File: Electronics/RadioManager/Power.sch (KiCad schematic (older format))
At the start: 10 parts

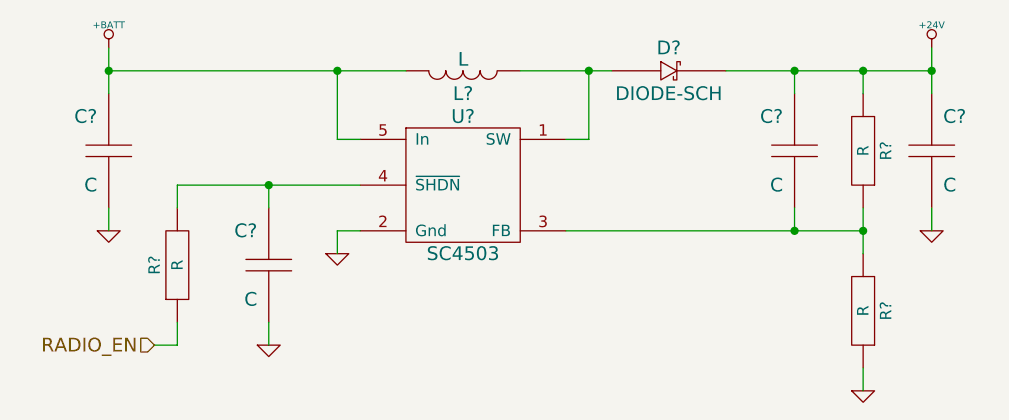
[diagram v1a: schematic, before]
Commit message: Annotate existing components
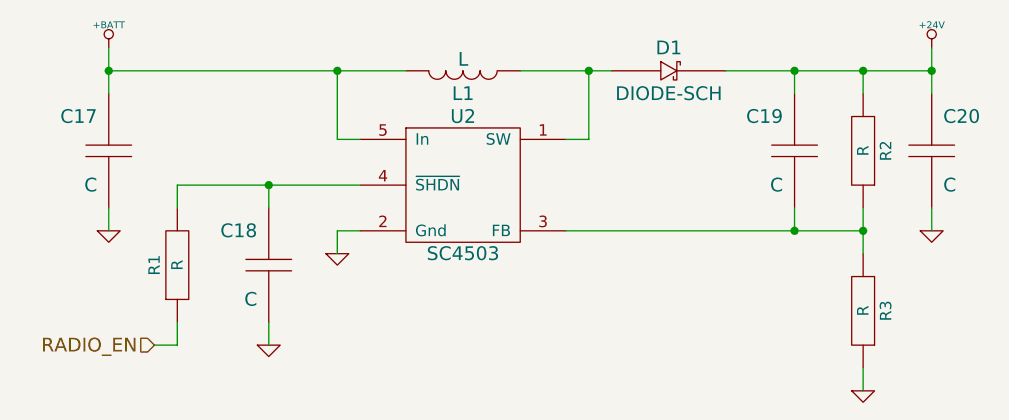
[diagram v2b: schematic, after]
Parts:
- gave numbers to parts that had none: 10
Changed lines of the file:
@@
 $EndDescr
 $Comp
-L SC4503 U?
+L SC4503 U2
 U 1 1 5410EB93
 P 3050 1900
-F 0 "U?" H 3050 2200 60  0000 C CNN
+F 0 "U2" H 3050 2200 60  0000 C CNN
 F 1 "SC4503" H 3050 1600 60  0000 C CNN
 F 2 "" H 3050 1900 60  0000 C CNN
@@
 $EndComp
 $Comp
-L L L?
+L L L1
 U 1 1 5410EB99
 P 3050 1400
-F 0 "L?" H 3050 1300 60  0000 C CNN
+F 0 "L1" H 3050 1300 60  0000 C CNN
 F 1 "L" H 3050 1450 60  0000 C CNN
 F 2 "~" H 3050 1400 60  0000 C CNN
@@
 $EndComp
 $Comp
-L DIODE-SCH D?
+L DIODE-SCH D1
 U 1 1 5410EB9F
 P 3950 1400
-F 0 "D?" H 3950 1500 60  0000 C CNN
+F 0 "D1" H 3950 1500 60  0000 C CNN
 F 1 "DIODE-SCH" H 3950 1300 60  0000 C CNN
 F 2 "~" H 3950 1400 60  0000 C CNN
@@
 $EndComp
 $Comp
-L R R?
+L R R2
 U 1 1 5410EBA7
 P 4800 1750
-F 0 "R?" H 4800 1850 50  0000 C CNN
+F 0 "R2" H 4800 1850 50  0000 C CNN
 F 1 "R" H 4800 1750 50  0000 C CNN
 F 2 "~" H 4800 1750 60  0000 C CNN
@@
 $EndComp
 $Comp
-L R R?
+L R R3
 U 1 1 5410EBAF
 P 4800 2450
-F 0 "R?" H 4800 2550 50  0000 C CNN
+F 0 "R3" H 4800 2550 50  0000 C CNN
 F 1 "R" H 4800 2450 50  0000 C CNN
 F 2 "~" H 4800 2450 60  0000 C CNN
@@
 $EndComp
 $Comp
-L C C?
+L C C19
 U 1 1 5410EBB7
 P 4500 1750
-F 0 "C?" H 4550 1900 60  0000 L CNN
+F 0 "C19" H 4550 1900 60  0000 L CNN
 F 1 "C" H 4550 1600 60  0000 L CNN
 F 2 "~" H 4500 1750 60  0000 C CNN
@@
 Connection ~ 4500 2100
 $Comp
-L C C?
+L C C20
 U 1 1 5410EBCC
 P 5100 1750
-F 0 "C?" H 5150 1900 60  0000 L CNN
+F 0 "C20" H 5150 1900 60  0000 L CNN
 F 1 "C" H 5150 1600 60  0000 L CNN
 F 2 "~" H 5100 1750 60  0000 C CNN
@@
 Connection ~ 4800 1400
 $Comp
-L +24V #PWR?
+L +24V #PWR35
 U 1 1 5410EBD4
 P 5100 1300
-F 0 "#PWR?" H 5100 1250 20  0001 C CNN
+F 0 "#PWR35" H 5100 1250 20  0001 C CNN
 F 1 "+24V" H 5100 1400 30  0000 C CNN
 F 2 "" H 5100 1300 60  0000 C CNN
@@
 Connection ~ 5100 1400
 $Comp
-L GND #PWR?
+L GND #PWR36
 U 1 1 5410EBDB
 P 5100 2100
-F 0 "#PWR?" H 5100 2100 30  0001 C CNN
+F 0 "#PWR36" H 5100 2100 30  0001 C CNN
 F 1 "GND" H 5100 2030 30  0001 C CNN
 F 2 "" H 5100 2100 60  0000 C CNN
@@
 $EndComp
 $Comp
-L GND #PWR?
+L GND #PWR34
 U 1 1 5410EBE1
 P 4800 2800
-F 0 "#PWR?" H 4800 2800 30  0001 C CNN
+F 0 "#PWR34" H 4800 2800 30  0001 C CNN
 F 1 "GND" H 4800 2730 30  0001 C CNN
 F 2 "" H 4800 2800 60  0000 C CNN
@@
 $EndComp
 $Comp
-L GND #PWR?
+L GND #PWR33
 U 1 1 5410EBE7
 P 2500 2200
-F 0 "#PWR?" H 2500 2200 30  0001 C CNN
+F 0 "#PWR33" H 2500 2200 30  0001 C CNN
 F 1 "GND" H 2500 2130 30  0001 C CNN
 F 2 "" H 2500 2200 60  0000 C CNN
@@
 	4800 2700 4800 2800
 $Comp
-L +BATT #PWR?
+L +BATT #PWR30
 U 1 1 5410EBF1
 P 1500 1300
-F 0 "#PWR?" H 1500 1250 20  0001 C CNN
+F 0 "#PWR30" H 1500 1250 20  0001 C CNN
 F 1 "+BATT" H 1500 1400 30  0000 C CNN
 F 2 "" H 1500 1300 60  0000 C CNN
@@
 	1500 1400 2800 1400
 $Comp
-L C C?
+L C C17
 U 1 1 5410EBFB
 P 1500 1750
-F 0 "C?" H 1550 1900 60  0000 L CNN
+F 0 "C17" H 1550 1900 60  0000 L CNN
 F 1 "C" H 1550 1600 60  0000 L CNN
 F 2 "~" H 1500 1750 60  0000 C CNN
@@
 $EndComp
 $Comp
-L GND #PWR?
+L GND #PWR31
 U 1 1 5410EC01
 P 1500 2100
-F 0 "#PWR?" H 1500 2100 30  0001 C CNN
+F 0 "#PWR31" H 1500 2100 30  0001 C CNN
 F 1 "GND" H 1500 2030 30  0001 C CNN
 F 2 "" H 1500 2100 60  0000 C CNN
@@
 Connection ~ 2500 1400
 $Comp
-L C C?
+L C C18
 U 1 1 5410EC0E
 P 2200 2250
-F 0 "C?" H 2250 2400 60  0000 L CNN
+F 0 "C18" H 2250 2400 60  0000 L CNN
 F 1 "C" H 2250 2100 60  0000 L CNN
 F 2 "~" H 2200 2250 60  0000 C CNN
@@
 $EndComp
 $Comp
-L R R?
+L R R1
 U 1 1 5410EC16
 P 1800 2250
-F 0 "R?" H 1800 2350 50  0000 C CNN
+F 0 "R1" H 1800 2350 50  0000 C CNN
 F 1 "R" H 1800 2250 50  0000 C CNN
 F 2 "~" H 1800 2250 60  0000 C CNN
@@
 Connection ~ 2200 1900
 $Comp
-L GND #PWR?
+L GND #PWR32
 U 1 1 5410EC20
 P 2200 2600
-F 0 "#PWR?" H 2200 2600 30  0001 C CNN
+F 0 "#PWR32" H 2200 2600 30  0001 C CNN
 F 1 "GND" H 2200 2530 30  0001 C CNN
 F 2 "" H 2200 2600 60  0000 C CNN

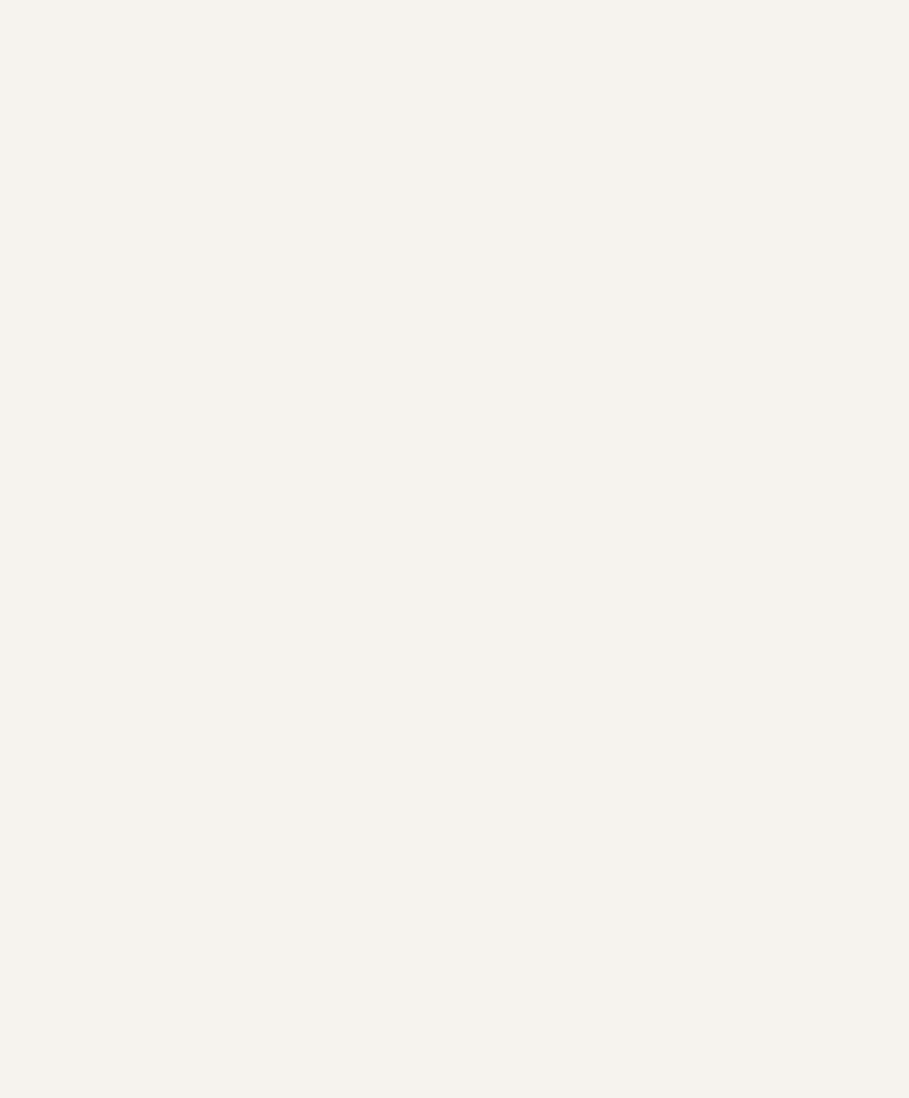
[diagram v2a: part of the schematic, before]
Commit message: Add 3v3 and 1v8 supplies
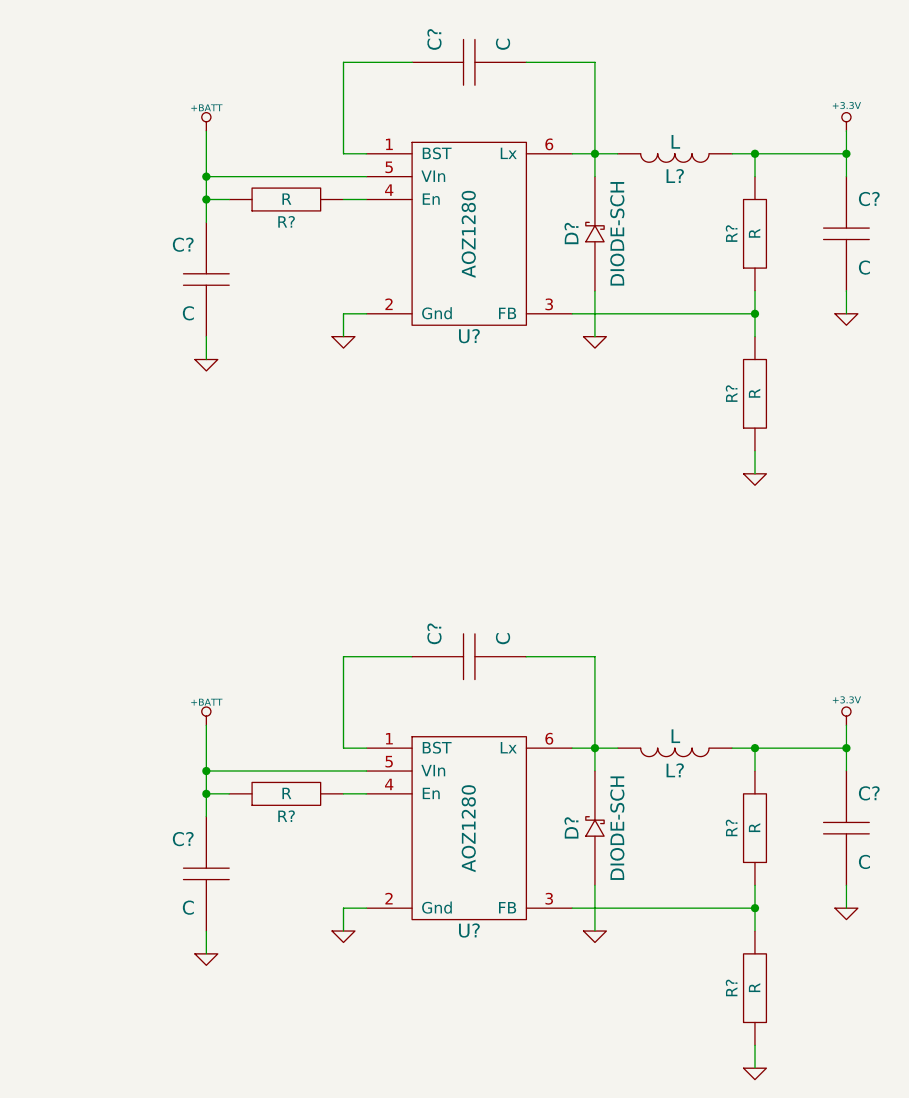
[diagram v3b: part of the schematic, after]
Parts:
- added C? (x6): C, ~, symbol C
- added D? (x2): DIODE-SCH, ~, symbol DIODE-SCH
- added L? (x2): L, ~, symbol L
- added R? (x6): R, ~, symbol R
- added U? (x2): AOZ1280, ~, symbol AOZ1280
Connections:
- net +BATT: now also C?.1, C?.1, R?.1, R?.1, U?.5 (VIn), U?.5 (VIn)
- net GND: now also C?.2, C?.2, C?.2, C?.2, D?.1, D?.1, R?.1, R?.1, U?.2 (Gnd), U?.2 (Gnd)
- new net: C?.1, U?.1 (BST) (x2)
- new net: R?.1, R?.2, U?.3 (FB) (x2)
- new net: R?.2, U?.4 (En) (x2)
- new net: C?.2, D?.2, L?.1, U?.6 (Lx) (x2)
- new net +3.3V: C?.1, C?.1, L?.2, L?.2, R?.2, R?.2

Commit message: Load new 3d models
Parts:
- gave numbers to parts that had none: 18
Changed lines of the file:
@@
 Sheet 3 3
 Title ""
-Date "14 sep 2014"
+Date "19 sep 2014"
 Rev ""
 Comp ""
@@
 Connection ~ 4800 1400
 $Comp
-L +24V #PWR35
+L +24V #PWR44
 U 1 1 5410EBD4
 P 5100 1300
-F 0 "#PWR35" H 5100 1250 20  0001 C CNN
+F 0 "#PWR44" H 5100 1250 20  0001 C CNN
 F 1 "+24V" H 5100 1400 30  0000 C CNN
 F 2 "" H 5100 1300 60  0000 C CNN
@@
 Connection ~ 5100 1400
 $Comp
-L GND #PWR36
+L GND #PWR45
 U 1 1 5410EBDB
 P 5100 2100
-F 0 "#PWR36" H 5100 2100 30  0001 C CNN
+F 0 "#PWR45" H 5100 2100 30  0001 C CNN
 F 1 "GND" H 5100 2030 30  0001 C CNN
 F 2 "" H 5100 2100 60  0000 C CNN
@@
 $EndComp
 $Comp
-L GND #PWR34
+L GND #PWR43
 U 1 1 5410EBE1
 P 4800 2800
-F 0 "#PWR34" H 4800 2800 30  0001 C CNN
+F 0 "#PWR43" H 4800 2800 30  0001 C CNN
 F 1 "GND" H 4800 2730 30  0001 C CNN
 F 2 "" H 4800 2800 60  0000 C CNN
@@
 $EndComp
 $Comp
-L GND #PWR33
+L GND #PWR42
 U 1 1 5410EBE7
 P 2500 2200
-F 0 "#PWR33" H 2500 2200 30  0001 C CNN
+F 0 "#PWR42" H 2500 2200 30  0001 C CNN
 F 1 "GND" H 2500 2130 30  0001 C CNN
 F 2 "" H 2500 2200 60  0000 C CNN
@@
 	4800 2700 4800 2800
 $Comp
-L +BATT #PWR30
+L +BATT #PWR39
 U 1 1 5410EBF1
 P 1500 1300
-F 0 "#PWR30" H 1500 1250 20  0001 C CNN
+F 0 "#PWR39" H 1500 1250 20  0001 C CNN
 F 1 "+BATT" H 1500 1400 30  0000 C CNN
 F 2 "" H 1500 1300 60  0000 C CNN
@@
 $EndComp
 $Comp
-L GND #PWR31
+L GND #PWR40
 U 1 1 5410EC01
 P 1500 2100
-F 0 "#PWR31" H 1500 2100 30  0001 C CNN
+F 0 "#PWR40" H 1500 2100 30  0001 C CNN
 F 1 "GND" H 1500 2030 30  0001 C CNN
 F 2 "" H 1500 2100 60  0000 C CNN
@@
 Connection ~ 2200 1900
 $Comp
-L GND #PWR32
+L GND #PWR41
 U 1 1 5410EC20
 P 2200 2600
-F 0 "#PWR32" H 2200 2600 30  0001 C CNN
+F 0 "#PWR41" H 2200 2600 30  0001 C CNN
 F 1 "GND" H 2200 2530 30  0001 C CNN
 F 2 "" H 2200 2600 60  0000 C CNN
@@
 RADIO_EN
 $Comp
-L AOZ1280 U?
+L AOZ1280 U4
 U 1 1 54160FAD
 P 8450 4650
-F 0 "U?" H 8450 4200 60  0000 C CNN
+F 0 "U4" H 8450 4200 60  0000 C CNN
 F 1 "AOZ1280" V 8450 4650 60  0000 C CNN
 F 2 "~" H 8450 5000 60  0000 C CNN
@@
 $EndComp
 $Comp
-L C C?
+L C C27
 U 1 1 54160FBC
 P 8450 3900
-F 0 "C?" H 8500 4050 60  0000 L CNN
+F 0 "C27" H 8500 4050 60  0000 L CNN
 F 1 "C" H 8500 3750 60  0000 L CNN
 F 2 "~" H 8450 3900 60  0000 C CNN
@@
 	8900 4300 9100 4300
 $Comp
-L L L?
+L L L3
 U 1 1 54161022
 P 9350 4300
-F 0 "L?" H 9350 4200 60  0000 C CNN
+F 0 "L3" H 9350 4200 60  0000 C CNN
 F 1 "L" H 9350 4350 60  0000 C CNN
 F 2 "~" H 9350 4300 60  0000 C CNN
@@
 $EndComp
 $Comp
-L R R?
+L R R14
 U 1 1 54161031
 P 9700 4650
-F 0 "R?" H 9700 4750 50  0000 C CNN
+F 0 "R14" H 9700 4750 50  0000 C CNN
 F 1 "R" H 9700 4650 50  0000 C CNN
 F 2 "~" H 9700 4650 60  0000 C CNN
@@
 $EndComp
 $Comp
-L R R?
+L R R15
 U 1 1 5416104C
 P 9700 5350
-F 0 "R?" H 9700 5450 50  0000 C CNN
+F 0 "R15" H 9700 5450 50  0000 C CNN
 F 1 "R" H 9700 5350 50  0000 C CNN
 F 2 "~" H 9700 5350 60  0000 C CNN
@@
 $EndComp
 $Comp
-L DIODE-SCH D?
+L DIODE-SCH D4
 U 1 1 54161067
 P 9000 4650
-F 0 "D?" H 9000 4750 60  0000 C CNN
+F 0 "D4" H 9000 4750 60  0000 C CNN
 F 1 "DIODE-SCH" H 9000 4550 60  0000 C CNN
 F 2 "~" H 9000 4650 60  0000 C CNN
@@
 Connection ~ 9000 4300
 $Comp
-L C C?
+L C C29
 U 1 1 541610C9
 P 10100 4650
-F 0 "C?" H 10150 4800 60  0000 L CNN
+F 0 "C29" H 10150 4800 60  0000 L CNN
 F 1 "C" H 10150 4500 60  0000 L CNN
 F 2 "~" H 10100 4650 60  0000 C CNN
@@
 Connection ~ 9700 4300
 $Comp
-L GND #PWR?
+L GND #PWR53
 U 1 1 541611C3
 P 9000 5100
-F 0 "#PWR?" H 9000 5100 30  0001 C CNN
+F 0 "#PWR53" H 9000 5100 30  0001 C CNN
 F 1 "GND" H 9000 5030 30  0001 C CNN
 F 2 "" H 9000 5100 60  0000 C CNN
@@
 $EndComp
 $Comp
-L GND #PWR?
+L GND #PWR55
 U 1 1 541611D2
 P 9700 5700
-F 0 "#PWR?" H 9700 5700 30  0001 C CNN
+F 0 "#PWR55" H 9700 5700 30  0001 C CNN
 F 1 "GND" H 9700 5630 30  0001 C CNN
 F 2 "" H 9700 5700 60  0000 C CNN
@@
 $EndComp
 $Comp
-L GND #PWR?
+L GND #PWR59
 U 1 1 541611E1
 P 10100 5000
-F 0 "#PWR?" H 10100 5000 30  0001 C CNN
+F 0 "#PWR59" H 10100 5000 30  0001 C CNN
 F 1 "GND" H 10100 4930 30  0001 C CNN
 F 2 "" H 10100 5000 60  0000 C CNN
@@
 	9700 5600 9700 5700
 $Comp
-L GND #PWR?
+L GND #PWR51
 U 1 1 54161286
 P 7900 5100
-F 0 "#PWR?" H 7900 5100 30  0001 C CNN
+F 0 "#PWR51" H 7900 5100 30  0001 C CNN
 F 1 "GND" H 7900 5030 30  0001 C CNN
 F 2 "" H 7900 5100 60  0000 C CNN
@@
 	7900 5000 8000 5000
 $Comp
-L R R?
+L R R11
 U 1 1 541612C9
 P 7650 4500
-F 0 "R?" H 7650 4600 50  0000 C CNN
+F 0 "R11" H 7650 4600 50  0000 C CNN
 F 1 "R" H 7650 4500 50  0000 C CNN
 F 2 "~" H 7650 4500 60  0000 C CNN
@@
 	8000 4500 7900 4500
 $Comp
-L C C?
+L C C25
 U 1 1 5416131A
 P 7300 4850
-F 0 "C?" H 7350 5000 60  0000 L CNN
+F 0 "C25" H 7350 5000 60  0000 L CNN
 F 1 "C" H 7350 4700 60  0000 L CNN
 F 2 "~" H 7300 4850 60  0000 C CNN
@@
 $EndComp
 $Comp
-L GND #PWR?
+L GND #PWR49
 U 1 1 54161335
 P 7300 5200
-F 0 "#PWR?" H 7300 5200 30  0001 C CNN
+F 0 "#PWR49" H 7300 5200 30  0001 C CNN
 F 1 "GND" H 7300 5130 30  0001 C CNN
 F 2 "" H 7300 5200 60  0000 C CNN
@@
 Connection ~ 7300 4500
 $Comp
-L +BATT #PWR?
+L +BATT #PWR48
 U 1 1 541613EB
 P 7300 4200
-F 0 "#PWR?" H 7300 4150 20  0001 C CNN
+F 0 "#PWR48" H 7300 4150 20  0001 C CNN
 F 1 "+BATT" H 7300 4300 30  0000 C CNN
 F 2 "" H 7300 4200 60  0000 C CNN
@@
 Connection ~ 7300 4400
 $Comp
-L +3.3V #PWR?
+L +3.3V #PWR58
 U 1 1 5416142F
 P 10100 4200
-F 0 "#PWR?" H 10100 4160 30  0001 C CNN
+F 0 "#PWR58" H 10100 4160 30  0001 C CNN
 F 1 "+3.3V" H 10100 4310 30  0000 C CNN
 F 2 "" H 10100 4200 60  0000 C CNN
@@
 Connection ~ 10100 4300
 $Comp
-L AOZ1280 U?
+L AOZ1280 U3
 U 1 1 54161496
 P 8450 2050
-F 0 "U?" H 8450 1600 60  0000 C CNN
+F 0 "U3" H 8450 1600 60  0000 C CNN
 F 1 "AOZ1280" V 8450 2050 60  0000 C CNN
 F 2 "~" H 8450 2400 60  0000 C CNN
@@
 $EndComp
 $Comp
-L C C?
+L C C26
 U 1 1 5416149E
 P 8450 1300
-F 0 "C?" H 8500 1450 60  0000 L CNN
+F 0 "C26" H 8500 1450 60  0000 L CNN
 F 1 "C" H 8500 1150 60  0000 L CNN
 F 2 "~" H 8450 1300 60  0000 C CNN
@@
 	8900 1700 9100 1700
 $Comp
-L L L?
+L L L2
 U 1 1 541614AA
 P 9350 1700
-F 0 "L?" H 9350 1600 60  0000 C CNN
+F 0 "L2" H 9350 1600 60  0000 C CNN
 F 1 "L" H 9350 1750 60  0000 C CNN
 F 2 "~" H 9350 1700 60  0000 C CNN
@@
 $EndComp
 $Comp
-L R R?
+L R R12
 U 1 1 541614B2
 P 9700 2050
-F 0 "R?" H 9700 2150 50  0000 C CNN
+F 0 "R12" H 9700 2150 50  0000 C CNN
 F 1 "R" H 9700 2050 50  0000 C CNN
 F 2 "~" H 9700 2050 60  0000 C CNN
@@
 $EndComp
 $Comp
-L R R?
+L R R13
 U 1 1 541614BA
 P 9700 2750
-F 0 "R?" H 9700 2850 50  0000 C CNN
+F 0 "R13" H 9700 2850 50  0000 C CNN
 F 1 "R" H 9700 2750 50  0000 C CNN
 F 2 "~" H 9700 2750 60  0000 C CNN
@@
 $EndComp
 $Comp
-L DIODE-SCH D?
+L DIODE-SCH D3
 U 1 1 541614C0
 P 9000 2050
-F 0 "D?" H 9000 2150 60  0000 C CNN
+F 0 "D3" H 9000 2150 60  0000 C CNN
 F 1 "DIODE-SCH" H 9000 1950 60  0000 C CNN
 F 2 "~" H 9000 2050 60  0000 C CNN
@@
 Connection ~ 9000 1700
 $Comp
-L C C?
+L C C28
 U 1 1 541614C9
 P 10100 2050
-F 0 "C?" H 10150 2200 60  0000 L CNN
+F 0 "C28" H 10150 2200 60  0000 L CNN
 F 1 "C" H 10150 1900 60  0000 L CNN
 F 2 "~" H 10100 2050 60  0000 C CNN
@@
 Connection ~ 9700 1700
 $Comp
-L GND #PWR?
+L GND #PWR52
 U 1 1 541614D6
 P 9000 2500
-F 0 "#PWR?" H 9000 2500 30  0001 C CNN
+F 0 "#PWR52" H 9000 2500 30  0001 C CNN
 F 1 "GND" H 9000 2430 30  0001 C CNN
 F 2 "" H 9000 2500 60  0000 C CNN
@@
 $EndComp
 $Comp
-L GND #PWR?
+L GND #PWR54
 U 1 1 541614DC
 P 9700 3100
-F 0 "#PWR?" H 9700 3100 30  0001 C CNN
+F 0 "#PWR54" H 9700 3100 30  0001 C CNN
 F 1 "GND" H 9700 3030 30  0001 C CNN
 F 2 "" H 9700 3100 60  0000 C CNN
@@
 $EndComp
 $Comp
-L GND #PWR?
+L GND #PWR57
 U 1 1 541614E2
 P 10100 2400
-F 0 "#PWR?" H 10100 2400 30  0001 C CNN
+F 0 "#PWR57" H 10100 2400 30  0001 C CNN
 F 1 "GND" H 10100 2330 30  0001 C CNN
 F 2 "" H 10100 2400 60  0000 C CNN
@@
 	9700 3000 9700 3100
 $Comp
-L GND #PWR?
+L GND #PWR50
 U 1 1 541614EB
 P 7900 2500
-F 0 "#PWR?" H 7900 2500 30  0001 C CNN
+F 0 "#PWR50" H 7900 2500 30  0001 C CNN
 F 1 "GND" H 7900 2430 30  0001 C CNN
 F 2 "" H 7900 2500 60  0000 C CNN
@@
 	7900 2400 8000 2400
 $Comp
-L R R?
+L R R10
 U 1 1 541614F5
 P 7650 1900
-F 0 "R?" H 7650 2000 50  0000 C CNN
+F 0 "R10" H 7650 2000 50  0000 C CNN
 F 1 "R" H 7650 1900 50  0000 C CNN
 F 2 "~" H 7650 1900 60  0000 C CNN
@@
 	8000 1900 7900 1900
 $Comp
-L C C?
+L C C24
 U 1 1 541614FE
 P 7300 2250
-F 0 "C?" H 7350 2400 60  0000 L CNN
+F 0 "C24" H 7350 2400 60  0000 L CNN
 F 1 "C" H 7350 2100 60  0000 L CNN
 F 2 "~" H 7300 2250 60  0000 C CNN
@@
 $EndComp
 $Comp
-L GND #PWR?
+L GND #PWR47
 U 1 1 54161504
 P 7300 2600
-F 0 "#PWR?" H 7300 2600 30  0001 C CNN
+F 0 "#PWR47" H 7300 2600 30  0001 C CNN
 F 1 "GND" H 7300 2530 30  0001 C CNN
 F 2 "" H 7300 2600 60  0000 C CNN
@@
 Connection ~ 7300 1900
 $Comp
-L +BATT #PWR?
+L +BATT #PWR46
 U 1 1 5416150F
 P 7300 1600
-F 0 "#PWR?" H 7300 1550 20  0001 C CNN
+F 0 "#PWR46" H 7300 1550 20  0001 C CNN
 F 1 "+BATT" H 7300 1700 30  0000 C CNN
 F 2 "" H 7300 1600 60  0000 C CNN
@@
 Connection ~ 7300 1800
 $Comp
-L +3.3V #PWR?
+L +3.3V #PWR56
 U 1 1 54161516
 P 10100 1600
-F 0 "#PWR?" H 10100 1560 30  0001 C CNN
+F 0 "#PWR56" H 10100 1560 30  0001 C CNN
 F 1 "+3.3V" H 10100 1710 30  0000 C CNN
 F 2 "" H 10100 1600 60  0000 C CNN
